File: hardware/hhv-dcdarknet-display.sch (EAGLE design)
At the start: 29 parts, among them IC1 7803

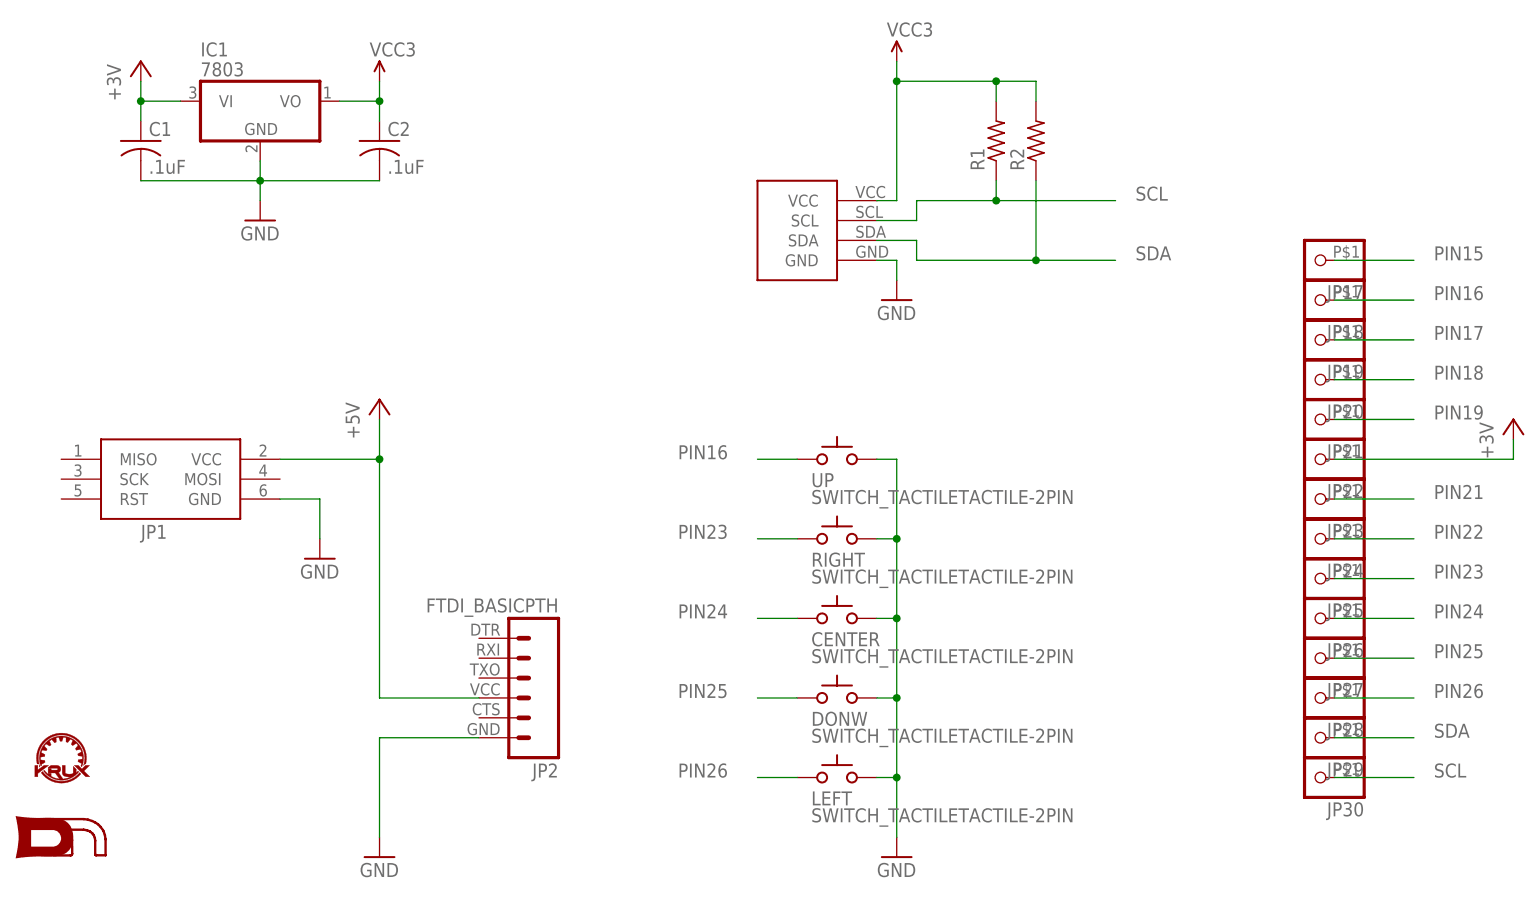
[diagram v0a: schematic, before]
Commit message: Updated Eagle files for the 2015 boards.
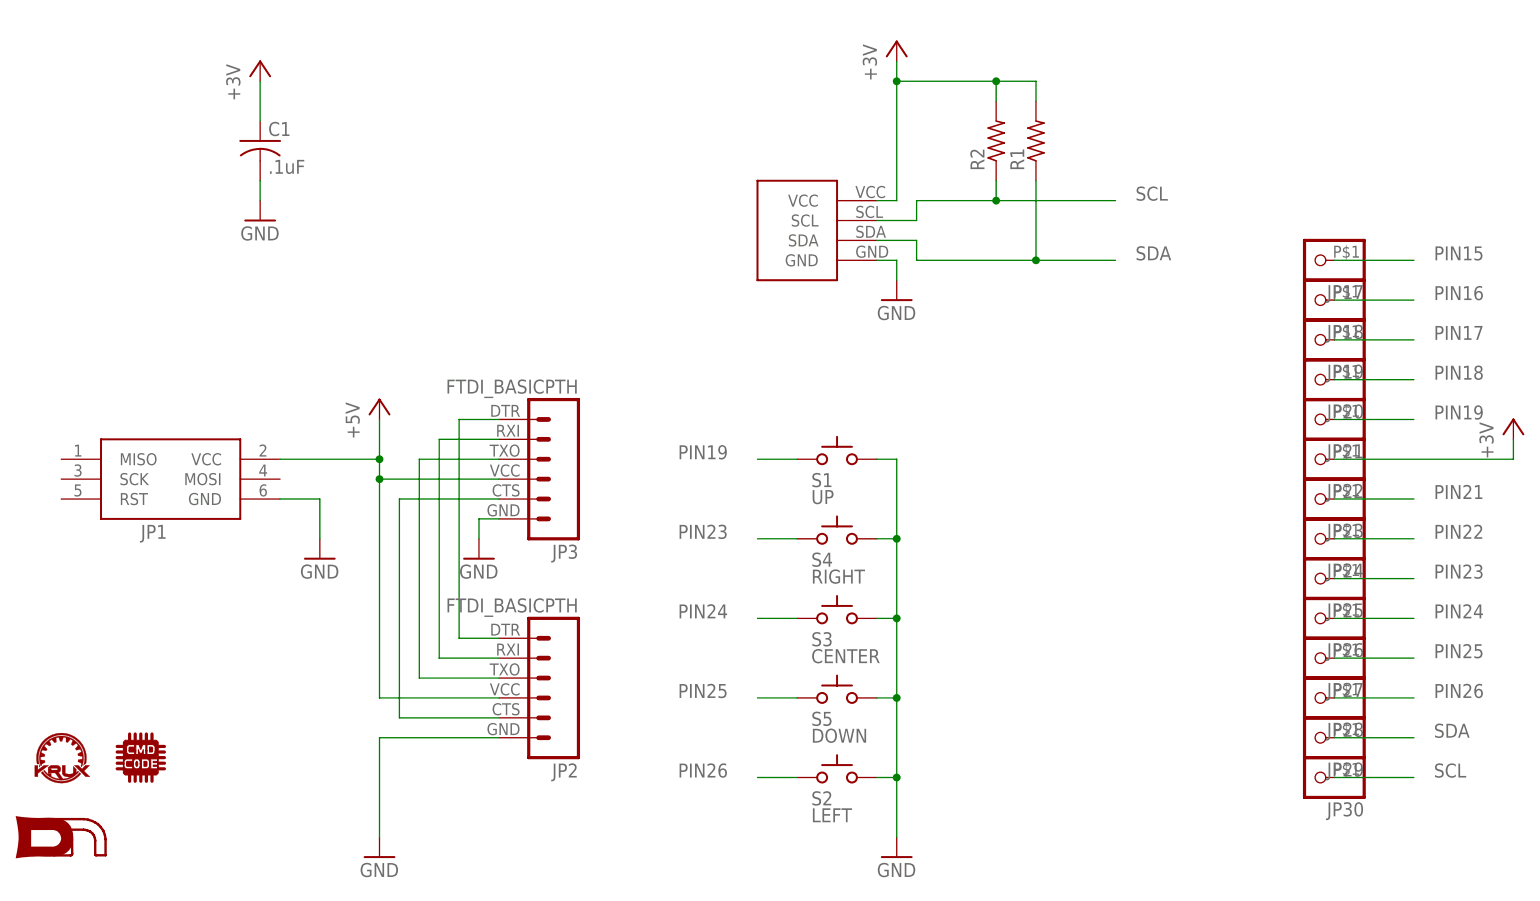
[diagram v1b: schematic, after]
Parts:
- removed C2: .1uF, adafruit:C-US025-030X050
- removed IC1: 7803, adafruit:7805L
- added JP3: FTDI_BASICPTH, SparkFun:FTDI_BASICPTH
- added U$4: CMDC0DE_LOGO, SYNShop:CMDC0DE_LOGO
- R1, R2: device SYNShop:R-US_0204/5 -> SYNShop:R-US_0204/7
- S1: value SWITCH_TACTILETACTILE-2PIN -> UP
- S2: value SWITCH_TACTILETACTILE-2PIN -> LEFT
- S3: value SWITCH_TACTILETACTILE-2PIN -> CENTER
- S4: value SWITCH_TACTILETACTILE-2PIN -> RIGHT
- S5: value SWITCH_TACTILETACTILE-2PIN -> DOWN
- renumbered CENTER to S3, DONW to S5, LEFT to S2, RIGHT to S4, UP to S1
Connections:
- removed net VCC3: C2.1, IC1.VO, R1.2, R2.2, U$3.VCC
- new net N$1: JP2.1, JP3.1
- new net N$2: JP2.2, JP3.2
- new net N$3: JP2.3, JP3.3
- new net N$4: JP2.5, JP3.5
- net +3V3: now also R1.2, R2.2, U$3.VCC; no longer IC1.VI
- net +5V: now also JP3.4
- net GND: now also JP3.6; no longer C2.2, IC1.GND
- net PIN16: no longer S1.C
- net PIN19: now also S1.C
- net PIN27: now also R1.1; no longer R2.1
- net PIN28: now also R2.1; no longer R1.1
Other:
- moved on the sheet: C1, JP2, R1, R2
